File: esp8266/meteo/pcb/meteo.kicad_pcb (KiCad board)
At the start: 2 copper layers, 33.3 x 44.7 mm, 4 parts

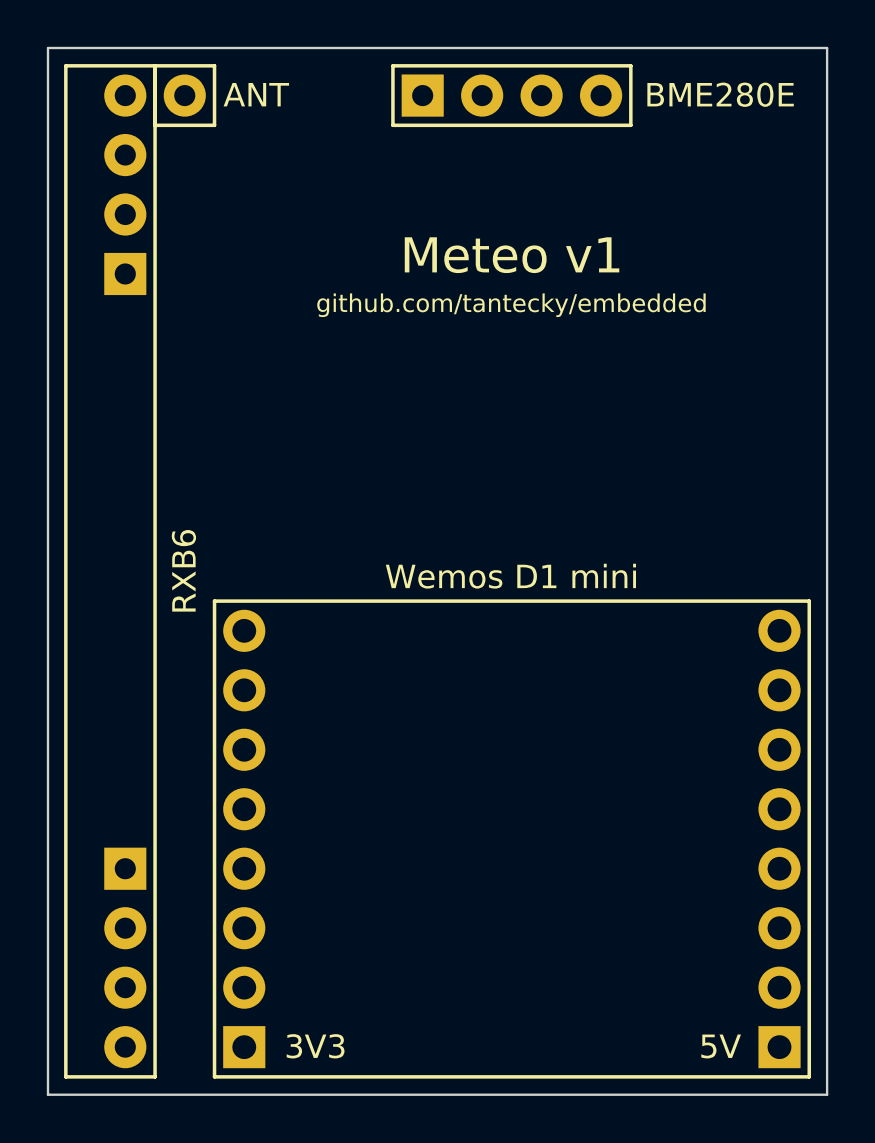
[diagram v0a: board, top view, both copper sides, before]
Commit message: meteo: Add tracks
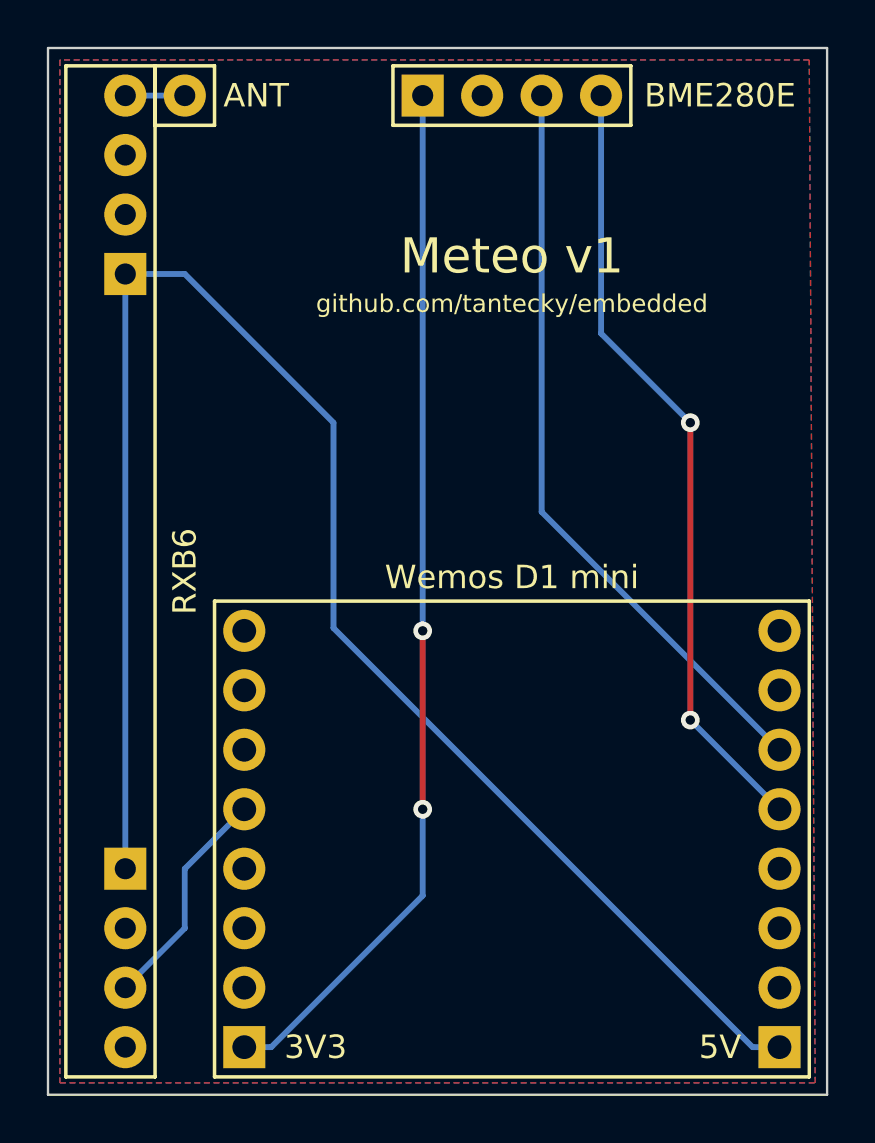
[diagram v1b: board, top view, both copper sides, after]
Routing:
- net Net-(U1-Pad1): track 0.00 -> 72.2 mm
- net Net-(U1-Pad16): track 0.00 -> 44.5 mm, vias 0 -> 2
- net Net-(U1-Pad5): track 0.00 -> 33.6 mm, vias 0 -> 2
- net Net-(U1-Pad6): track 0.00 -> 32.1 mm
- net Net-(U1-Pad12): track 0.00 -> 9.72 mm
- net Net-(AE1-Pad1): track 0.00 -> 2.54 mm
- added copper zone on B.Cu, net GND
- added copper zone on F.Cu, net GND
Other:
- net class Default: via_dia 1 -> 0.8; via_drill 0.5 -> 0.4
- rule trace_min: 0.2 -> 0.25
- rule via_min_drill: 0.3 -> 0.4
- rule via_min_size: 0.4 -> 0.8
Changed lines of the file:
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@@
     (thickness 1.6)
     (drawings 6)
-    (tracks 0)
+    (tracks 26)
     (zones 0)
     (modules 4)
@@
     (47 F.CrtYd user)
     (48 B.Fab user)
-    (49 F.Fab user)
+    (49 F.Fab user hide)
   )
   (setup
@@
     (zone_clearance 0.508)
     (zone_45_only no)
-    (trace_min 0.2)
+    (trace_min 0.25)
     (segment_width 0.2)
     (edge_width 0.1)
-    (via_size 1)
-    (via_drill 0.5)
-    (via_min_size 0.4)
-    (via_min_drill 0.3)
+    (via_size 0.8)
+    (via_drill 0.4)
+    (via_min_size 0.8)
+    (via_min_drill 0.4)
     (uvia_size 0.3)
     (uvia_drill 0.1)
@@
     (pad_to_mask_clearance 0)
     (aux_axis_origin 0 0)
-    (visible_elements FFFFF77F)
+    (visible_elements FFFFFF7F)
     (pcbplotparams
-      (layerselection 0x010fc_ffffffff)
+      (layerselection 0x010f0_ffffffff)
       (usegerberextensions false)
       (usegerberattributes false)
@@
       (outputformat 1)
       (mirror false)
-      (drillshape 1)
+      (drillshape 0)
       (scaleselection 1)
-      (outputdirectory ""))
+      (outputdirectory "gerbs/"))
   )
   (net 0 "")
@@
     (clearance 0.25)
     (trace_width 0.25)
-    (via_dia 1)
-    (via_drill 0.5)
+    (via_dia 0.8)
+    (via_drill 0.4)
     (uvia_dia 0.3)
     (uvia_drill 0.1)
+    (diff_pair_gap 0.25)
+    (diff_pair_width 0.25)
     (add_net GND)
     (add_net "Net-(AE1-Pad1)")
@@
   (gr_line (start 167.132 150.622) (end 167.132 105.918) (layer Edge.Cuts) (width 0.1))
   (gr_line (start 133.858 150.622) (end 167.132 150.622) (layer Edge.Cuts) (width 0.1))
+  (segment (start 137.16 107.95) (end 139.7 107.95) (width 0.25) (layer B.Cu) (net 1))
+  (segment (start 139.7 140.97) (end 142.24 138.43) (width 0.25) (layer B.Cu) (net 5))
+  (segment (start 139.7 143.51) (end 139.7 140.97) (width 0.25) (layer B.Cu) (net 5))
+  (segment (start 137.16 146.05) (end 139.7 143.51) (width 0.25) (layer B.Cu) (net 5))
+  (via (at 149.86 138.43) (size 0.8) (drill 0.4) (layers F.Cu B.Cu) (net 9))
+  (segment (start 149.86 142.12) (end 149.86 138.43) (width 0.25) (layer B.Cu) (net 9))
+  (segment (start 143.39 148.59) (end 149.86 142.12) (width 0.25) (layer B.Cu) (net 9))
+  (segment (start 142.24 148.59) (end 143.39 148.59) (width 0.25) (layer B.Cu) (net 9))
+  (segment (start 149.86 138.43) (end 149.86 130.81) (width 0.25) (layer F.Cu) (net 9))
+  (segment (start 149.86 130.81) (end 149.86 130.81) (width 0.25) (layer F.Cu) (net 9))
+  (via (at 149.86 130.81) (size 0.8) (drill 0.4) (layers F.Cu B.Cu) (net 9))
+  (segment (start 149.86 107.95) (end 149.86 130.81) (width 0.25) (layer B.Cu) (net 9))
+  (segment (start 137.16 140.97) (end 137.16 115.57) (width 0.25) (layer B.Cu) (net 10))
+  (segment (start 165.1 148.59) (end 163.95 148.59) (width 0.25) (layer B.Cu) (net 10))
+  (segment (start 163.95 148.59) (end 146.05 130.69) (width 0.25) (layer B.Cu) (net 10))
+  (segment (start 146.05 130.69) (end 146.05 121.92) (width 0.25) (layer B.Cu) (net 10))
+  (segment (start 139.7 115.57) (end 137.16 115.57) (width 0.25) (layer B.Cu) (net 10))
+  (segment (start 146.05 121.92) (end 139.7 115.57) (width 0.25) (layer B.Cu) (net 10))
+  (segment (start 165.1 138.43) (end 161.29 134.62) (width 0.25) (layer B.Cu) (net 14))
+  (via (at 161.29 134.62) (size 0.8) (drill 0.4) (layers F.Cu B.Cu) (net 14))
+  (segment (start 161.29 134.62) (end 161.29 121.92) (width 0.25) (layer F.Cu) (net 14))
+  (segment (start 157.48 118.11) (end 157.48 107.95) (width 0.25) (layer B.Cu) (net 14))
+  (segment (start 161.29 121.92) (end 157.48 118.11) (width 0.25) (layer B.Cu) (net 14))
+  (via (at 161.29 121.92) (size 0.8) (drill 0.4) (layers F.Cu B.Cu) (net 14))
+  (segment (start 154.94 125.73) (end 154.94 107.95) (width 0.25) (layer B.Cu) (net 15))
+  (segment (start 165.1 135.89) (end 154.94 125.73) (width 0.25) (layer B.Cu) (net 15))
+  (zone (net 11) (net_name GND) (layer B.Cu) (hatch edge 0.508)
+    (connect_pads (clearance 0.508))
+    (min_thickness 0.254)
+    (fill yes (arc_segments 16) (thermal_gap 0.508) (thermal_bridge_width 0.508))
+    (polygon
+      (pts
+        (xy 166.624 150.114) (xy 166.37 106.426) (xy 134.366 106.426) (xy 134.366 150.114)
+      )
+    )
+  )
+  (zone (net 11) (net_name GND) (layer F.Cu) (hatch edge 0.508)
+    (connect_pads (clearance 0.508))
+    (min_thickness 0.254)
+    (fill yes (arc_segments 16) (thermal_gap 0.508) (thermal_bridge_width 0.508))
+    (polygon
+      (pts
+        (xy 166.624 150.114) (xy 166.37 106.426) (xy 134.366 106.426) (xy 134.366 150.114)
+      )
+    )
+  )
 )

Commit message: meteo: Add a logo
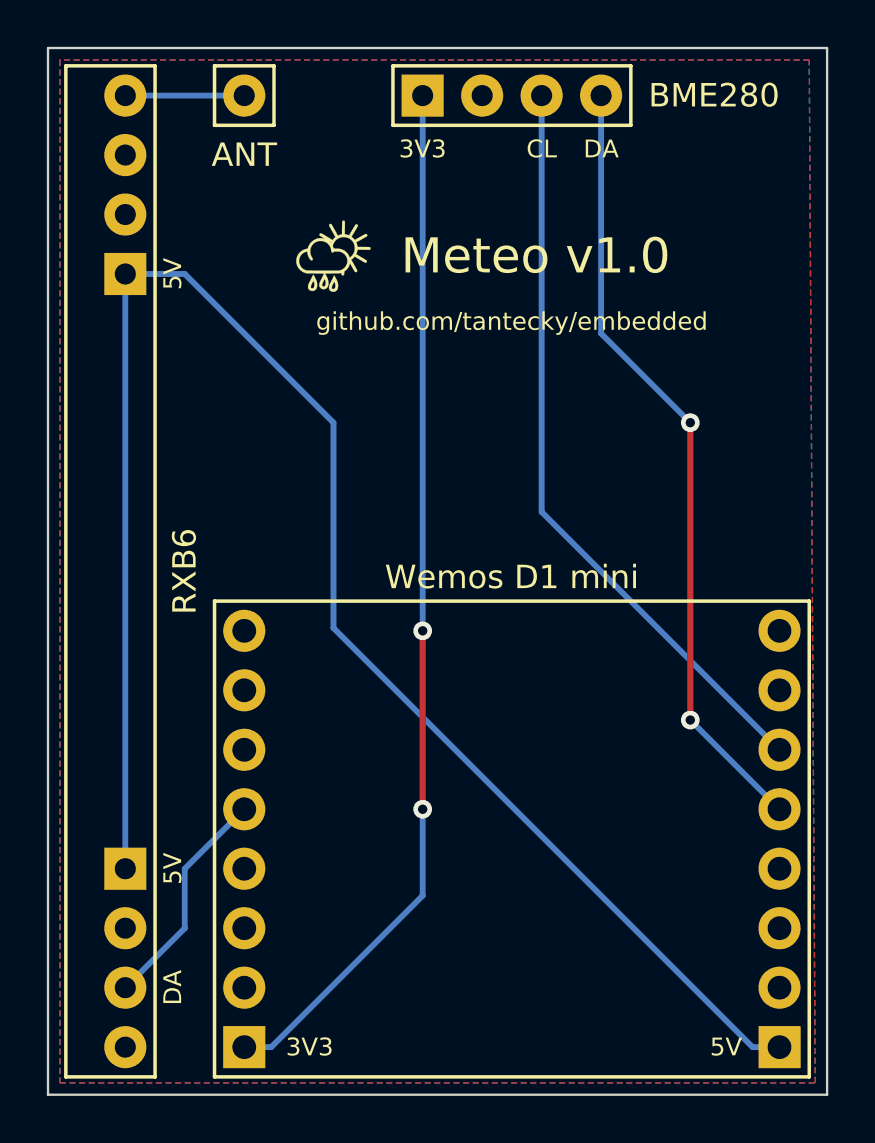
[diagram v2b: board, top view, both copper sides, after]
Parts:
- added G***: LOGO, meteo:logo, F.Cu at (146.1, 114.8)
- moved ANT 2.54 mm to (142.2, 108.0)
- renumbered BME280E to BME280
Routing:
- net Net-(AE1-Pad1): track 2.54 -> 5.08 mm
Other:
- board text added: "3V3"
- board text added: "5V"
- board text added: "CL"
- board text added: "DA"
- board text added: "Meteo v1.0"
- board text removed: "Meteo v1"
